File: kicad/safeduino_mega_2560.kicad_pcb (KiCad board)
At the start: 4 copper layers, 134.5 x 63.9 mm, 109 parts, among them X1 USBB-1J

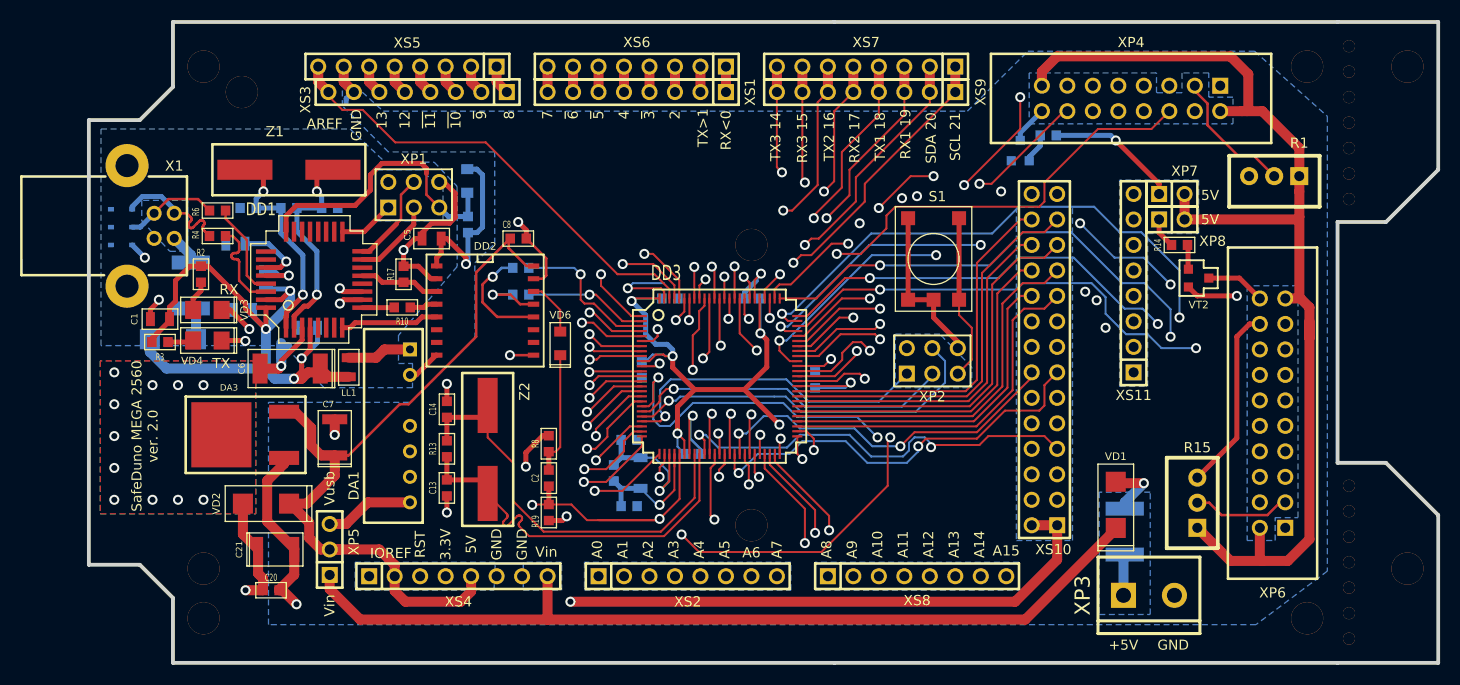
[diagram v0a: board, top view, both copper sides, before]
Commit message: Продолжил оптимизацию трассировки печатной платы.
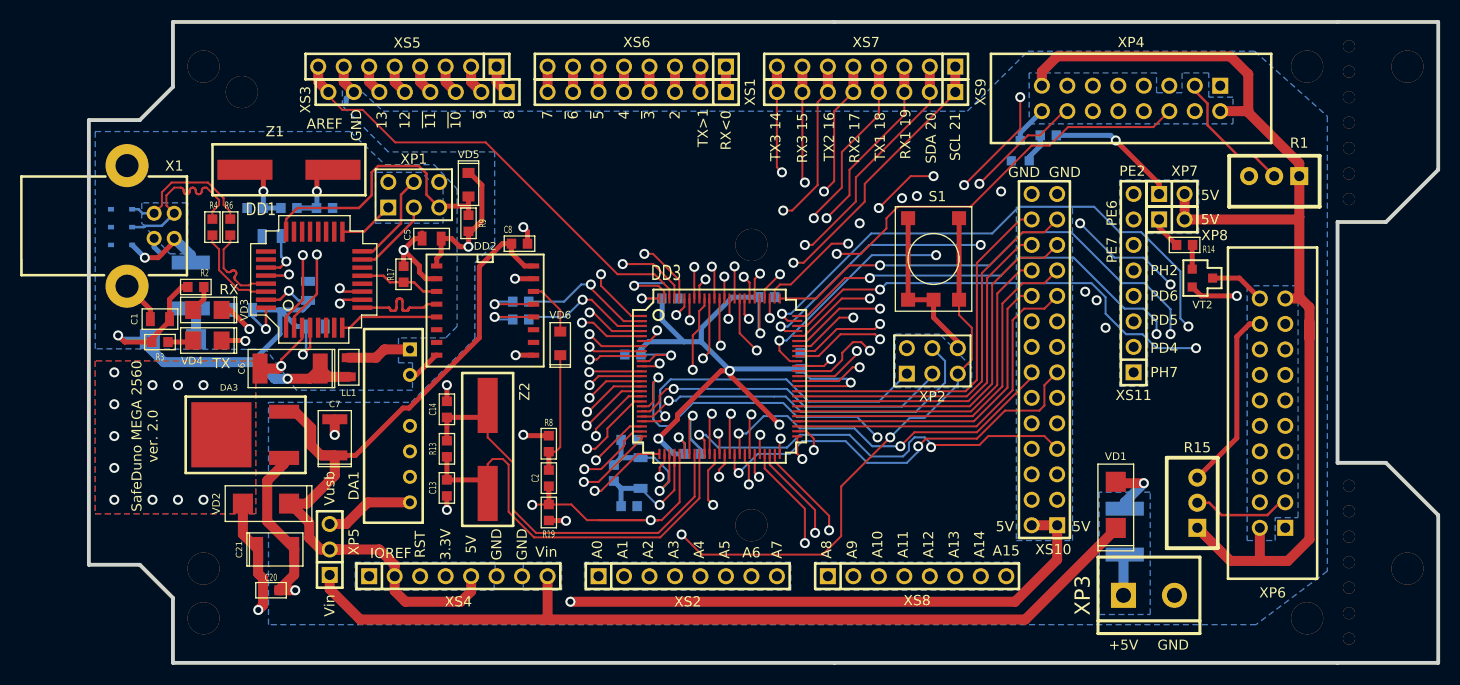
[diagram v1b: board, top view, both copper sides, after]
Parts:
- removed R10: 47, IWsmd_case:SMD0603
- R9, VD5: moved to F.Cu
- moved R11 5.14 mm to (95.1, 119.2)
- moved C12 4.34 mm to (73.9, 116.3)
- moved C10 3.69 mm to (70.3, 110.9)
- moved C17 2.40 mm to (123.0, 123.3)
- moved R6 2.08 mm to (66.2, 110.0), turned to 270 degrees
- moved VD10 1.78 mm to (56.4, 108.2)
- moved VD9 1.78 mm to (56.4, 110.0)
- moved C15 1.77 mm to (106.3, 122.7), turned to 180 degrees
- moved C18 1.40 mm to (119.6, 117.0), turned to 0 degrees
- moved R2 1.37 mm to (62.7, 116.0), turned to 180 degrees
- moved R4 1.03 mm to (64.4, 110.0), turned to 270 degrees
- moved C9 0.77 mm to (74.7, 119.9), turned to 180 degrees
- moved R12 0.70 mm to (95.1, 117.4)
- moved C3 0.69 mm to (68.6, 108.1)
- moved C8 0.52 mm to (95.0, 111.6)
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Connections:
- DD2 pad 4: Net-(DD2-Pad4) -> /PE0
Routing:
- net /GND: track 101.9 -> 84.4 mm, vias 14 -> 15
- net /MPU_VCC: track 381.5 -> 393.8 mm, vias 7 -> 9
- net /GND_USB: track 37.4 -> 28.7 mm, vias 4 -> 3
- net /5V_USB: track 129.6 -> 122.8 mm, vias 5 -> 6
- net /PE0: track 3.19 -> 9.97 mm
- net Net-(DD2-Pad12): track 11.0 -> 5.79 mm
- net /USB_D+: track 9.34 -> 14.3 mm
- net /USB_D-: track 12.4 -> 16.7 mm
- net /RESET: track 100.4 -> 104.4 mm
- net /PD7: track 35.3 -> 31.4 mm
- net /ADC1: track 46.8 -> 43.5 mm
- net /PG1: track 32.1 -> 29.1 mm
- net /PG0: track 35.6 -> 32.8 mm
- net Net-(DD2-Pad4): track 2.77 -> 0.00 mm
- net Net-(C13-Pad1): track 42.5 -> 45.1 mm
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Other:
- board text added: "PD4"
- board text added: "PD5"
- board text added: "PD6"
- board text added: "PE2"
- board text added: "PE6"
- board text added: "PE7"
- board text added: "PH2"
- board text added: "PH7"

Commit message: Поправил схему для лучшей защиты от ЭМП и продолжил переделывать трассировку печатной платы.
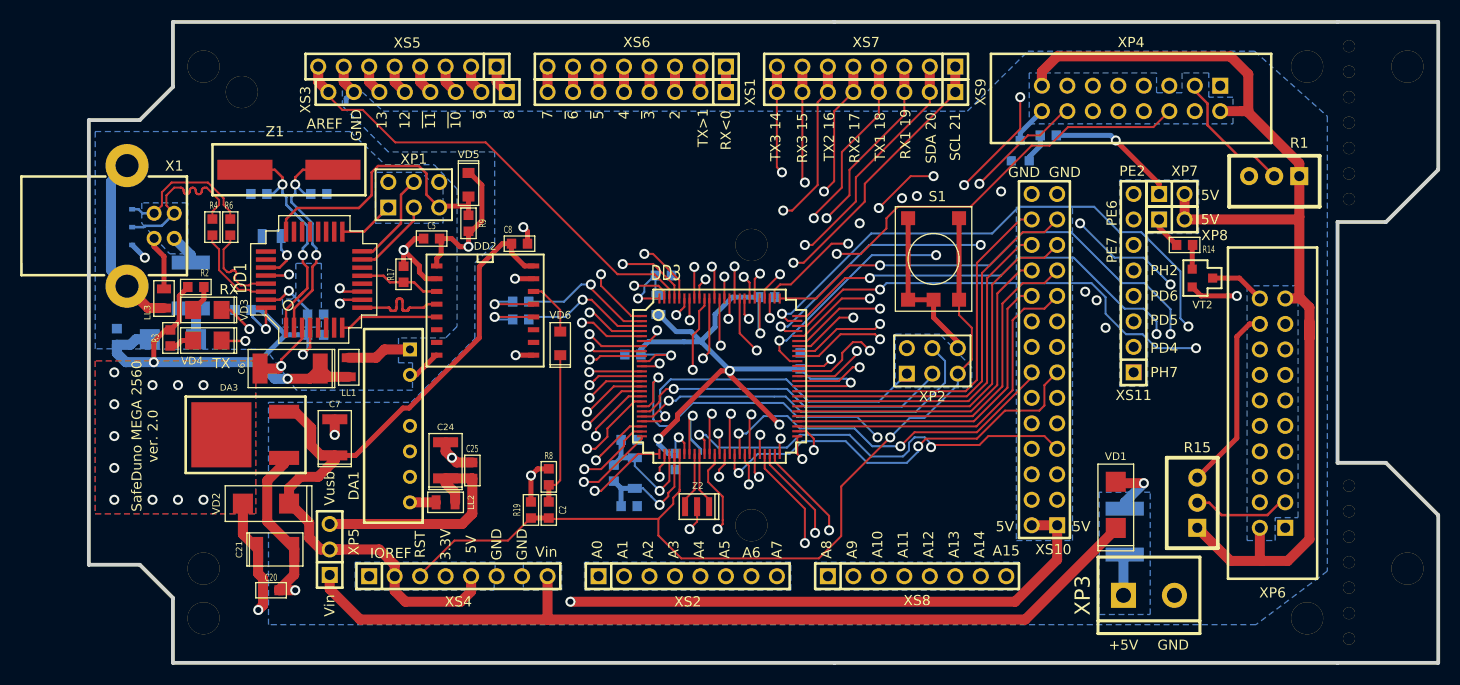
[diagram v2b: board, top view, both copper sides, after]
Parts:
- removed C13, C14: 22п, IWsmd_case:SMD0603
- removed R13, R7: 1M, IWsmd_case:SMD0603
- added C24: 22мк 10В, IWsmd_case:CASE_B, F.Cu at (87.6, 133.2)
- added C25: 0.1мк, IWsmd_case:SMD0603, F.Cu at (90.3, 134.2)
- added LL2: MMZ2012R601AT000, IWsmd_case:SMD0805, F.Cu at (87.6, 137.4)
- added LL3: MMZ2012R600A, IWsmd_case:SMD0805, F.Cu at (59.6, 117.1)
- added LL4: LQM21FN100N00L, IWsmd_case:SMD0805, B.Cu at (108.8, 117.7)
- C1: footprint IWsmd_case:SMD0805 -> IWsmd_case:SMD0603; moved to B.Cu
- C11, C12, C5, C9: footprint IWsmd_case:SMD0805 -> IWsmd_case:SMD0603
- C6: value 4.7 мк 50В -> 10 мк 25В
- C7: value 47мк 10В -> 22мк 10В
- LL1: value MMZ2012R601AT000 -> MMZ2012R600A
- Z2: value 16МГц -> CSTCE16M0V53-R0; footprint IWcomponents:HC-49SM -> IWsmd_case:CSTNE_G_8-13_99MHz
- moved Z2 21.6 mm to (112.7, 137.8), turned to 180 degrees
- moved C1 4.64 mm to (54.9, 120.9), turned to 90 degrees
- moved R8 3.30 mm to (97.9, 134.9)
- moved C2 3.18 mm to (97.9, 138.2)
- moved C12 2.47 mm to (74.7, 118.7), turned to 180 degrees
- moved C19 2.37 mm to (109.3, 114.8)
- moved C16 1.88 mm to (110.6, 133.3), turned to 270 degrees
- moved R19 1.80 mm to (96.1, 138.2), turned to 270 degrees
- moved C4 1.51 mm to (75.0, 106.7)
- moved C3 1.45 mm to (69.0, 106.7)
- moved R3 1.11 mm to (60.2, 121.0), turned to 90 degrees
- moved C9 0.83 mm to (74.7, 120.7)
- moved Z3 0.58 mm to (106.5, 134.5)
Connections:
- net /D+ renamed /RD+
- net /D- renamed /RD-
- C19 pad 1: /MPU_VCC -> Net-(C19-Pad1)
- DA1 pad 7: /VCCUSB -> Net-(DA1-Pad7)
- DD3 pad 100: /MPU_VCC -> Net-(C19-Pad1)
- DD3 pad 33: Net-(C14-Pad1) -> Net-(DD3-Pad33)
- DD3 pad 34: Net-(C13-Pad1) -> Net-(DD3-Pad34)
- VD10 pad 2: /GND_USB -> Net-(LL3-Pad2)
- VD7 pad 2: /GND_USB -> Net-(LL3-Pad2)
- VD9 pad 2: /GND_USB -> Net-(LL3-Pad2)
- X1 pad 5: /GND_USB -> Net-(LL3-Pad2)
- X1 pad 6: /GND_USB -> Net-(LL3-Pad2)
- Z2 pad 1: Net-(C14-Pad1) -> Net-(DD3-Pad34)
- Z2 pad 2: Net-(C13-Pad1) -> /GND
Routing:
- net Net-(C13-Pad1): track 45.1 -> 0.00 mm
- net Net-(C14-Pad1): track 41.9 -> 0.00 mm
- net Net-(LL3-Pad2): track 0.00 -> 18.0 mm
- net /VCCUSB: track 8.90 -> 23.6 mm
- net /RESET: track 104.4 -> 94.2 mm, vias 4 -> 1
- net Net-(C19-Pad1): track 0.00 -> 7.28 mm, vias 0 -> 1
- net Net-(DD3-Pad34): track 0.00 -> 5.66 mm
- net Net-(DD3-Pad33): track 0.00 -> 5.65 mm
- net /MPU_VCC: track 393.8 -> 389.6 mm, vias 9 -> 8
- net Net-(C2-Pad2): track 12.3 -> 15.6 mm
- net /PG3: track 15.6 -> 12.6 mm
- net Net-(DA1-Pad7): track 0.00 -> 2.60 mm
- net /5V_USB: track 122.8 -> 121.1 mm
- net /GND: track 84.4 -> 85.3 mm, vias 15 -> 14
- net Net-(C4-Pad1): track 20.4 -> 21.2 mm
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
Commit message: Продолжил оптимизировать трассировку печатной платы.
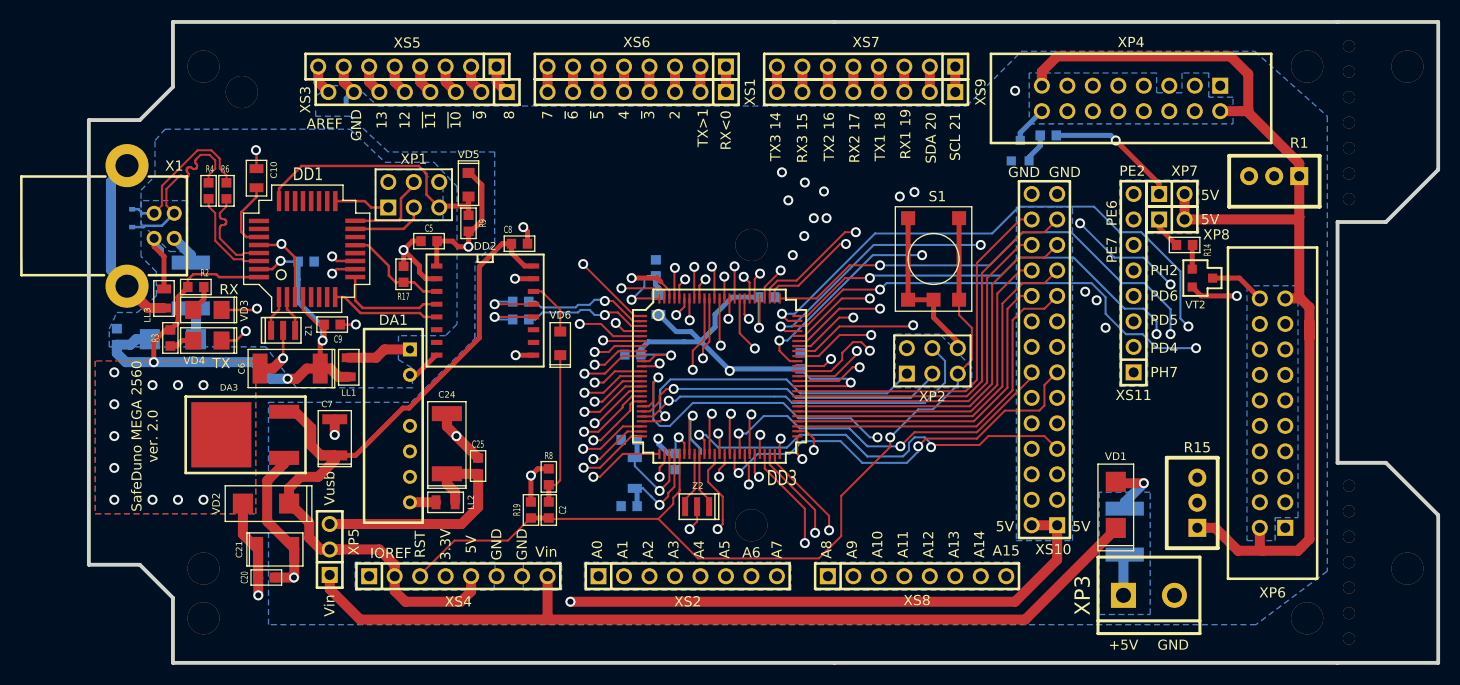
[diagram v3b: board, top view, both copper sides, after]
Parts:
- removed C12: 0.1мк, IWsmd_case:SMD0603
- removed C3, C4: 22п, IWsmd_case:SMD0603
- removed R18: 1M, IWsmd_case:SMD0603
- removed VD7: PESD5V0L1BA,115, IWcomponents:SOD323
- C10, C9: moved to F.Cu
- C24: value 22мк 10В -> 47мк 10В; footprint IWsmd_case:CASE_B -> IWsmd_case:CASE_C
- Z1: value 16МГц -> CSTCE16M0V53-R0; footprint IWcomponents:HC-49SM -> IWsmd_case:CSTNE_G_8-13_99MHz
- moved Z1 16.0 mm to (71.4, 120.3)
- moved C11 7.92 mm to (73.7, 113.4), turned to 180 degrees
- moved C10 5.96 mm to (68.8, 105.1), turned to 270 degrees
- moved R4 3.64 mm to (64.0, 106.4)
- moved R6 3.64 mm to (65.8, 106.4)
- moved DD1 3.13 mm to (73.9, 112.1)
- moved C9 1.94 mm to (76.3, 119.7)
- moved C24 1.66 mm to (87.8, 131.6)
- moved C20 1.36 mm to (69.8, 144.9)
- moved C19 1.08 mm to (108.6, 114.0), turned to 90 degrees
- moved C25 0.72 mm to (90.9, 133.8)
- moved C5 0.36 mm to (86.0, 111.4)
- turned C22 to 180 degrees
- turned C23 to 180 degrees
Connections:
- DD1 pad 2: Net-(C4-Pad1) -> Net-(DD1-Pad2)
- Z1 pad 2: Net-(C4-Pad1) -> /GND_USB
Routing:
- net Net-(C4-Pad1): track 21.2 -> 0.00 mm, vias 2 -> 0
- net Net-(DD1-Pad1): track 22.2 -> 3.64 mm, vias 2 -> 0
- net /ADC1: track 43.5 -> 34.7 mm
- net /GND_USB: track 29.3 -> 36.9 mm, vias 3 -> 5
- net /PE7: track 76.0 -> 82.6 mm
- net Net-(FU1-Pad1): track 9.63 -> 3.09 mm, vias 1 -> 0
- net /PE4: track 29.0 -> 35.1 mm
- net /PA0: track 83.8 -> 78.5 mm, vias 3 -> 2
- net /PJ5: track 39.8 -> 44.7 mm, vias 2 -> 1
- net /PH1: track 50.5 -> 55.4 mm
- net /5V_USB: track 121.1 -> 125.8 mm, vias 6 -> 5
- net /PJ7: track 49.2 -> 53.8 mm, vias 2 -> 1
- net Net-(DD1-Pad2): track 0.00 -> 3.65 mm
- net /PH0: track 51.7 -> 55.2 mm
- net /SS: track 54.9 -> 58.4 mm
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
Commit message: Продолжил оптимизировать трассировку печатной платы.
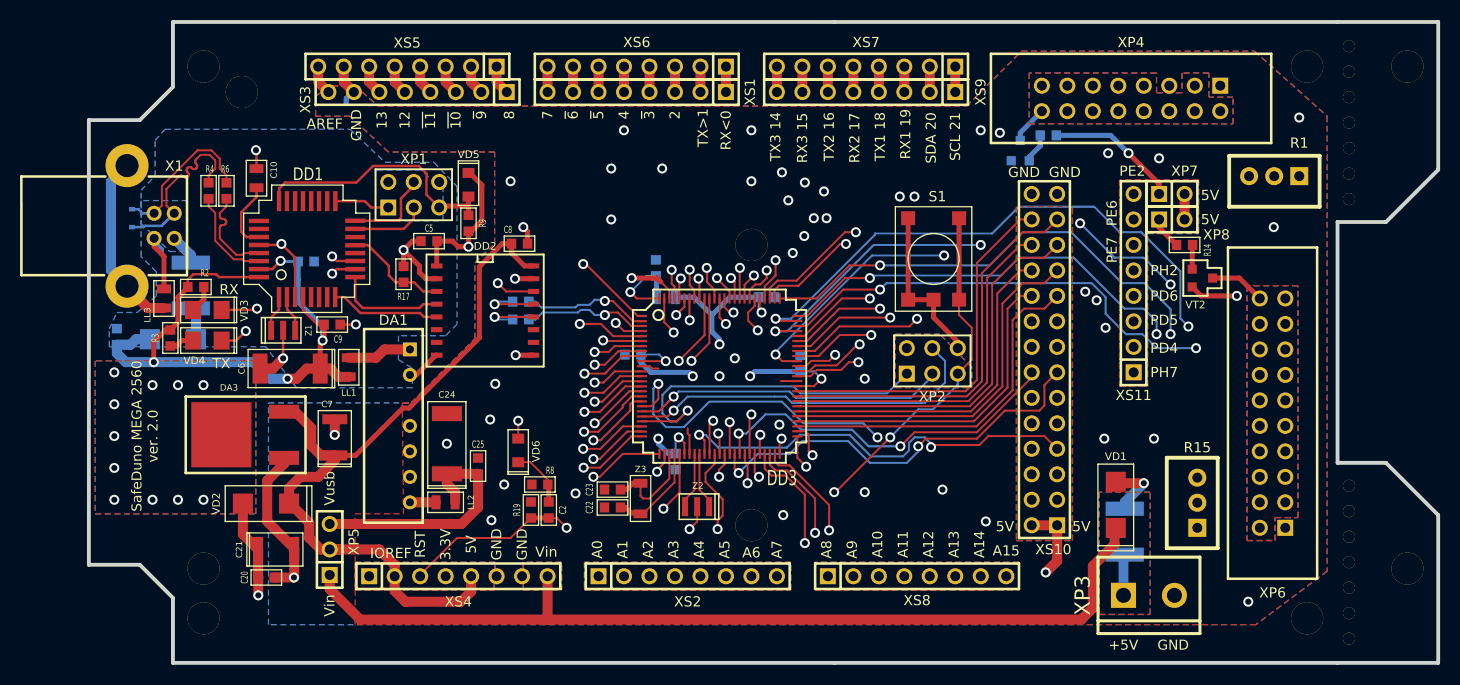
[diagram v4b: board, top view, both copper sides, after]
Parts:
- C22, C23, Z3: moved to F.Cu
- moved VD6 11.5 mm to (94.9, 131.1)
- moved C23 5.22 mm to (104.3, 136.1)
- moved Z3 2.60 mm to (107.1, 137.0)
- moved C22 1.66 mm to (104.3, 137.9)
- moved R8 1.17 mm to (97.0, 135.6), turned to 0 degrees
- moved LL4 1.08 mm to (109.6, 117.0), turned to 180 degrees
- moved C17 0.25 mm to (123.0, 123.6)
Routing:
- net /GND: track 86.6 -> 64.7 mm, vias 14 -> 38
- net Net-(DD2-Pad14): track 5.58 -> 20.2 mm, vias 0 -> 2
- net Net-(C2-Pad2): track 15.6 -> 5.93 mm
- net /ADC6: track 31.0 -> 39.6 mm
- net /ADC7: track 31.9 -> 40.2 mm
- net /ADC13: track 36.6 -> 44.7 mm
- net /ADC5: track 34.4 -> 42.1 mm
- net /ADC11: track 35.0 -> 42.6 mm
- net /MPU_VCC: track 389.5 -> 383.0 mm, vias 7 -> 9
- net /ADC14: track 37.4 -> 43.8 mm
- net /RESET: track 93.2 -> 87.4 mm, vias 1 -> 4
- net /PL3: track 49.7 -> 44.2 mm
- net /PH7: track 75.0 -> 69.8 mm
- net /PJ1: track 53.7 -> 49.3 mm
- net /PD7: track 31.4 -> 35.8 mm
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- added copper zone on F.Cu, net /GND

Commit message: Продолжил оптимизировать трассировку печатной платы.
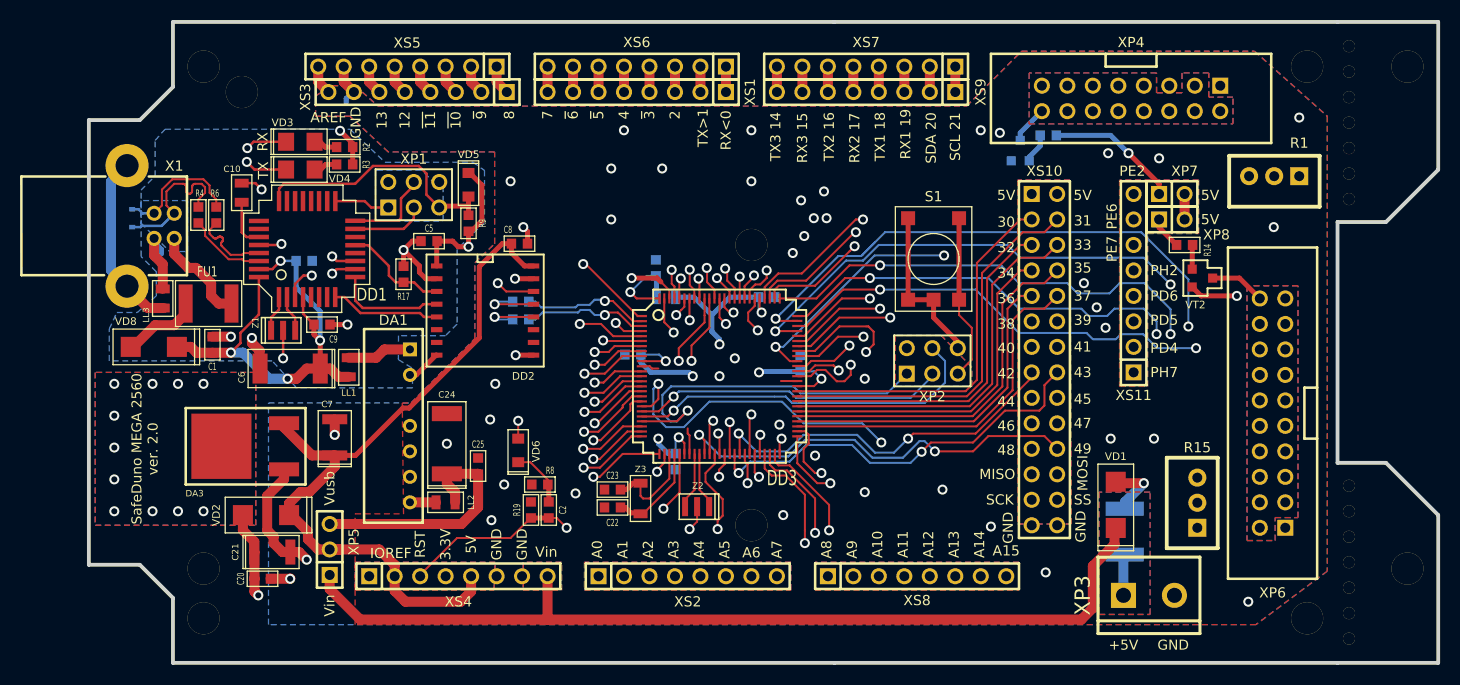
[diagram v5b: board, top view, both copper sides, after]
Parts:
- C1, FU1, VD8: moved to F.Cu
- moved R3 24.5 mm to (77.6, 103.7), turned to 0 degrees
- moved R2 20.4 mm to (77.6, 102.0), turned to 0 degrees
- moved VD4 19.4 mm to (73.2, 104.2), turned to 180 degrees
- moved VD3 19.2 mm to (73.2, 101.5), turned to 180 degrees
- moved C1 9.56 mm to (64.4, 121.7)
- moved R6 2.62 mm to (64.8, 108.8)
- moved R4 2.62 mm to (63.0, 108.8)
- moved XS10 2.54 mm to (148.6, 123.2), turned to 270 degrees
- moved FU1 2.53 mm to (64.0, 117.6), turned to 180 degrees
- moved C10 2.07 mm to (67.3, 106.6)
- moved VD8 2.05 mm to (58.5, 121.9), turned to 0 degrees
- moved DA3 1.14 mm to (71.6, 131.8)
- moved VD2 1.14 mm to (69.7, 138.7)
- moved C9 1.02 mm to (75.3, 119.7)
- moved C21 0.46 mm to (70.4, 142.4)
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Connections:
- XS10 pad 10: /PL3 -> /PC0
- XS10 pad 11: /PL4 -> /PD7
- XS10 pad 12: /PL5 -> /PG2
- XS10 pad 13: /PL6 -> /PG1
- XS10 pad 14: /PL7 -> /PG0
- XS10 pad 15: /PG0 -> /PL7
- XS10 pad 16: /PG1 -> /PL6
- XS10 pad 17: /PG2 -> /PL5
- XS10 pad 18: /PD7 -> /PL4
- XS10 pad 19: /PC0 -> /PL3
- XS10 pad 20: /PC1 -> /PL2
- XS10 pad 21: /PC2 -> /PL1
- XS10 pad 22: /PC3 -> /PL0
- XS10 pad 23: /PC4 -> /MISO
- XS10 pad 24: /PC5 -> /MOSI
- XS10 pad 25: /PC6 -> /SCK
- XS10 pad 26: /PC7 -> /SS
- XS10 pad 3: /SS -> /PC7
- XS10 pad 4: /SCK -> /PC6
- XS10 pad 5: /MOSI -> /PC5
- XS10 pad 6: /MISO -> /PC4
- XS10 pad 7: /PL0 -> /PC3
- XS10 pad 8: /PL1 -> /PC2
- XS10 pad 9: /PL2 -> /PC1
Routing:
- net /PJ1: track 49.3 -> 38.9 mm, vias 3 -> 1
- net /MPU_VCC: track 383.0 -> 392.4 mm
- net /RXI: track 15.0 -> 23.4 mm
- net /5V_USB: track 125.8 -> 117.8 mm, vias 5 -> 6
- net Net-(FU1-Pad1): track 3.09 -> 10.1 mm
- net /PJ0: track 47.8 -> 41.4 mm, vias 3 -> 1
- net Net-(FU1-Pad2): track 3.29 -> 7.86 mm
- net /PJ5: track 41.1 -> 45.3 mm
- net /SS: track 57.5 -> 53.7 mm
- net /USB_D-: track 18.1 -> 15.3 mm
- net /USB_D+: track 15.7 -> 12.9 mm
- net /ADC12: track 42.5 -> 45.3 mm
- net /PG1: track 32.9 -> 35.1 mm
- net Net-(C10-Pad2): track 7.00 -> 4.90 mm
- net /VCC3V3: track 31.0 -> 29.1 mm
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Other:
- board text added: "30"
- board text added: "31"
- board text added: "32"
- board text added: "33"
- board text added: "34"
- board text added: "35"
- board text added: "36"
- board text added: "37"
- board text added: "38"
- board text added: "39"
- board text added: "40"
- board text added: "41"
- board text added: "42"
- board text added: "43"
- board text added: "44"
- board text added: "45"
- board text added: "46"
- board text added: "47"
- board text added: "48"
- board text added: "49"
- board text added: "MISO"
- board text added: "MOSI"
- board text added: "SCK"
- board text added: "SS"
